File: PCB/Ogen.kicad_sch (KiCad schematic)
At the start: 17 parts, among them J1 Input, U1 PMW3360DM-T2QU, U2 TLV70019, U3 TXS0102DCU, U4 TXS0102DCU, U5 TXS0102DCU

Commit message: V1.2 update.
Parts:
- removed C1: 4.7uF, Capacitor_SMD:C_0603_1608Metric, symbol Device:C_Small
- removed C2: 100nF, Capacitor_SMD:C_0603_1608Metric, symbol Device:C_Small
- removed C3, C4: 1uF, Capacitor_SMD:C_0603_1608Metric, symbol Device:C_Small
- removed R1, R2: 10k, Resistor_SMD:R_0603_1608Metric, symbol Device:R_Small
- removed R3: 39R, Resistor_SMD:R_0603_1608Metric, symbol Device:R_Small
- removed U2: TLV70019, Package_TO_SOT_SMD:SOT-23-5, symbol Regulator_Linear:TLV70019_SOT23-5
- added C22 (x2): 1u, Capacitor_SMD:C_0402_1005Metric, symbol Device:C_Small
- added C93: 4u7, Capacitor_SMD:C_0603_1608Metric, symbol Device:C_Small
- added C94: 100n, Capacitor_SMD:C_0402_1005Metric, symbol Device:C_Small
- added R10, R14, R27: 10k, Resistor_SMD:R_0402_1005Metric, symbol Device:R_Small
- added R11: 39, Resistor_SMD:R_0402_1005Metric, symbol Device:R_Small
- added R28: 15k, Resistor_SMD:R_0402_1005Metric, symbol Device:R_Small
- added U6: AP2127K-ADJ, Package_TO_SOT_SMD:SOT-23-5, symbol Regulator_Linear:AP2127K-ADJ
- A1: footprint Ogen:Ariamelon_Logo -> Ogen:Ariamelon_Logo-CU; symbol Mechanical:MountingHole -> Mechanical:Fiducial
- U3, U4, U5: LCSC (none) -> C53434
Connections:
- net GND: now also C22.2, C22.2, C93.2, C94.1, R27.2, U6.2 (GND)
- net NRESET: now also R10.1
- net VCC: now also C22.1, U6.1 (VIN), U6.3 (EN)
- net at U1.3 (VDDPIX): now also C93.1, C94.2
- net at U1.15 (LED_P): now also R11.1
- net at JP1.1 (A): now also R14.2
- net VDD renamed +2V
- net +2V: now also C22.1, R10.2, R11.2, R14.1, R28.1, U6.5 (VOUT)
- new net: R27.1, R28.2, U6.4 (ADJ)
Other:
- moved on the sheet: H1, H2, J1, JP1, U1, U3, U4, U5

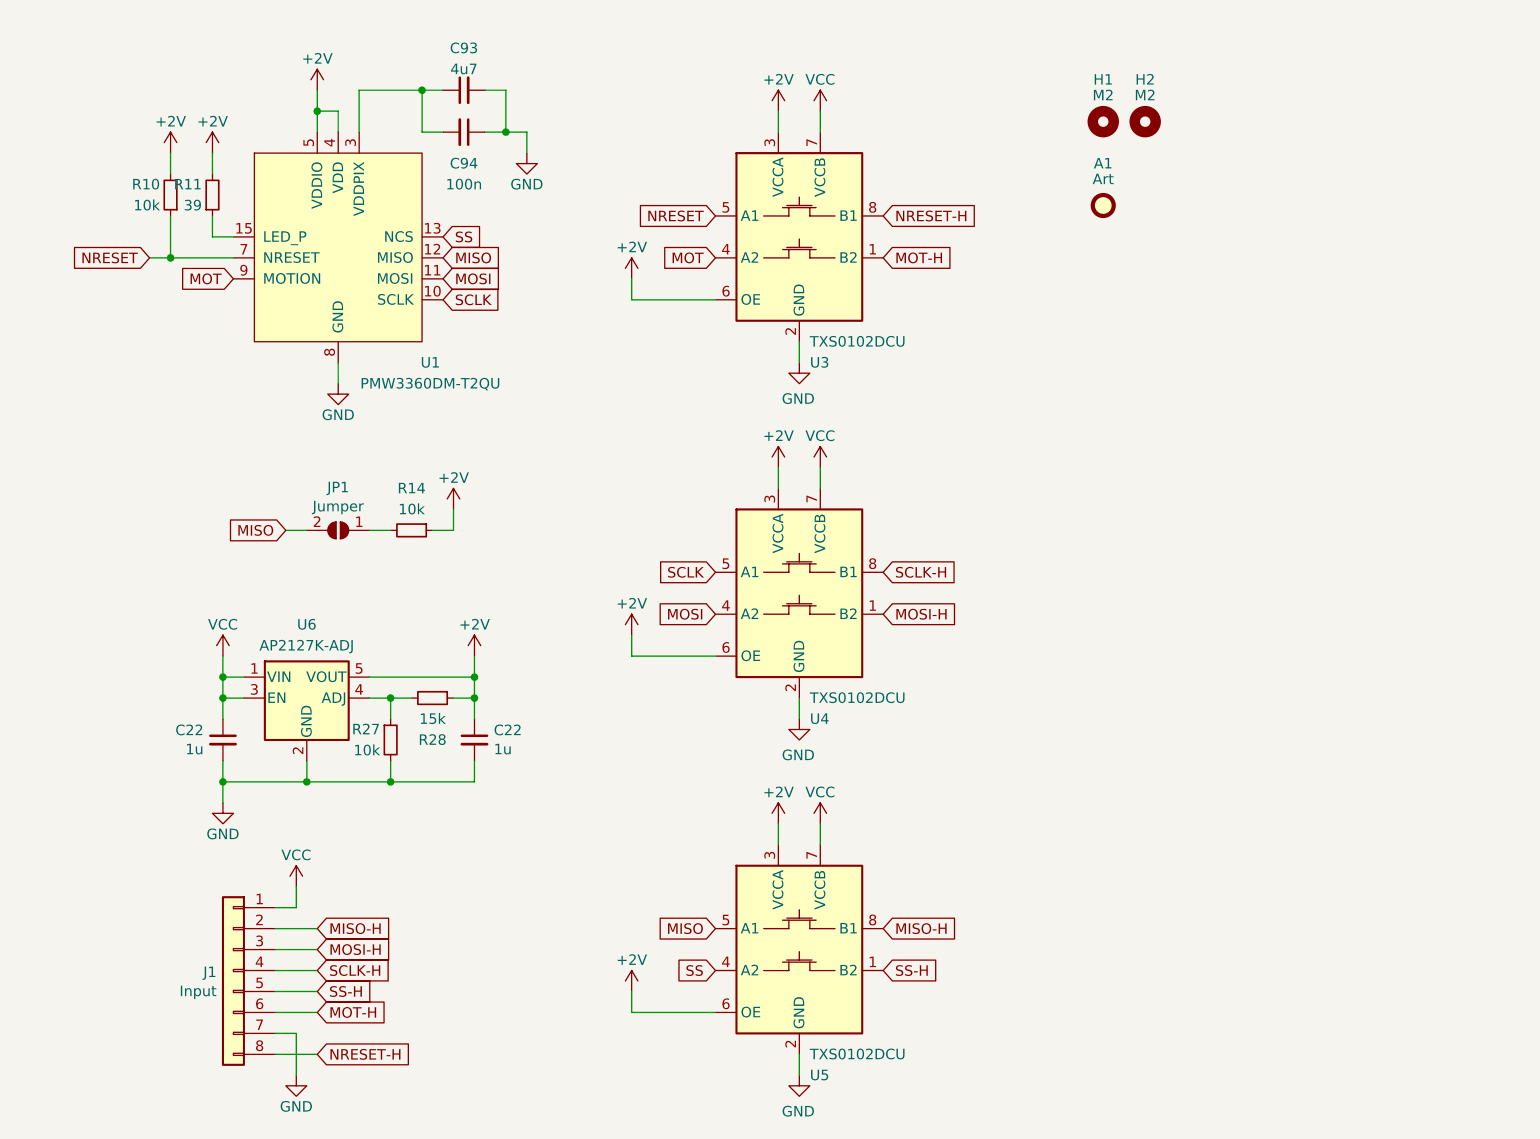
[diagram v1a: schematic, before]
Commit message: 04/08/2023 update
Updated to V1.3. Changed all parts back to 0603. Stitched ground planes together. Removed MISO pullup jumper (MISO is pulled up by default now). Added metadata to schematic and PCB file. Changed location of production files for easier access.
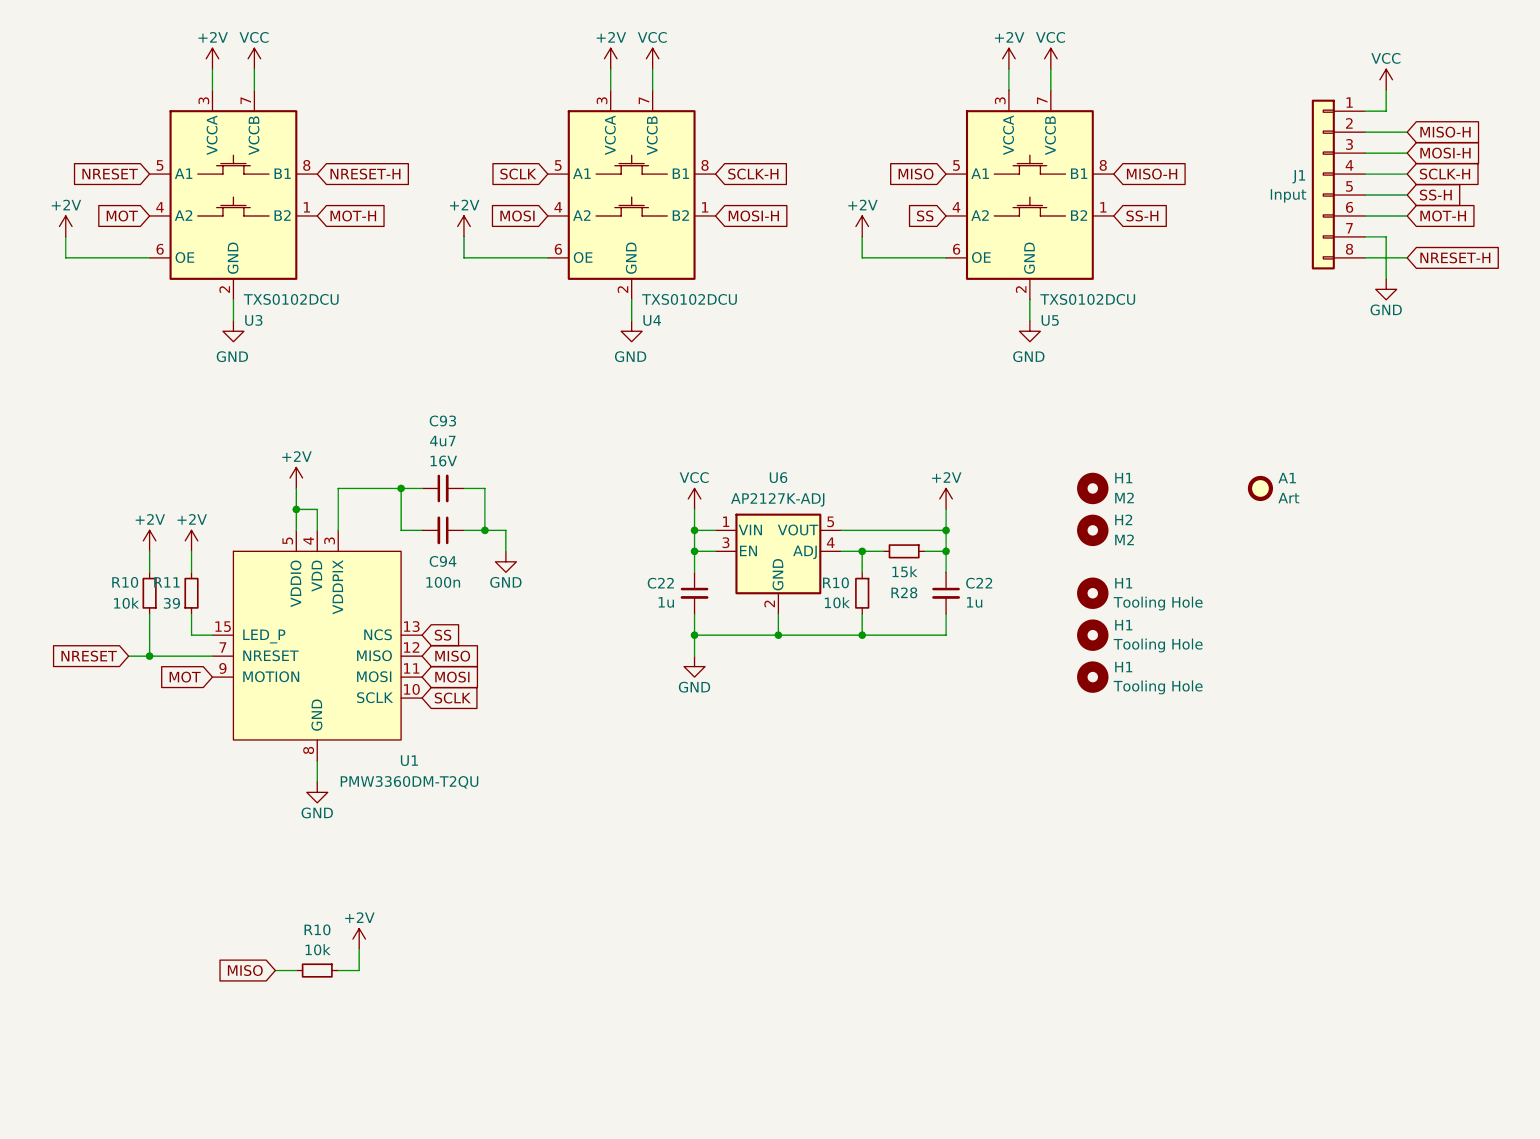
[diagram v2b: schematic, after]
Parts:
- removed JP1: Jumper, Jumper:SolderJumper-2_P1.3mm_Open_Pad1.0x1.5mm, symbol Jumper:SolderJumper_2_Open
- removed R14, R27: 10k, Resistor_SMD:R_0402_1005Metric, symbol Device:R_Small
- added H1 (x3): Tooling Hole, Ogen:JLC Tooling Hole, symbol Mechanical:MountingHole
- added R10 (x2): 10k, Resistor_SMD:R_0603_1608Metric, symbol Device:R_Small
- A1, H1, H2, J1: now left out of the parts list
- C22: footprint Capacitor_SMD:C_0402_1005Metric -> Capacitor_SMD:C_0603_1608Metric; LCSC C52923 -> C15849
- C93: Voltage (none) -> 16V
- C94: footprint Capacitor_SMD:C_0402_1005Metric -> Capacitor_SMD:C_0603_1608Metric; LCSC C1525 -> C14663
- R10: footprint Resistor_SMD:R_0402_1005Metric -> Resistor_SMD:R_0603_1608Metric; LCSC C25744 -> C25804
- R11: footprint Resistor_SMD:R_0402_1005Metric -> Resistor_SMD:R_0603_1608Metric; LCSC C25164 -> C25236
- R28: footprint Resistor_SMD:R_0402_1005Metric -> Resistor_SMD:R_0603_1608Metric; LCSC C25756 -> C22809
- U3, U4, U5: footprint Package_SO:VSSOP-8_2.3x2mm_P0.5mm -> Ogen:VSSOP-8_2.3x2mm_P0.5mm
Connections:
- net +2V: now also R10.1
- net GND: now also R10.2
- net MISO: now also R10.2
- net at R28.2, U6.4 (ADJ): now also R10.1
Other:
- company: (none) -> Created by Ariamelon (https://github.com/Ariamelon/Ogen/tree/V1.3)
- title: (none) -> Ogen PMW3360 Module
- moved on the sheet: A1, C22, C93, C94, H1, H2, J1, R10, R11, R28, U1, U3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

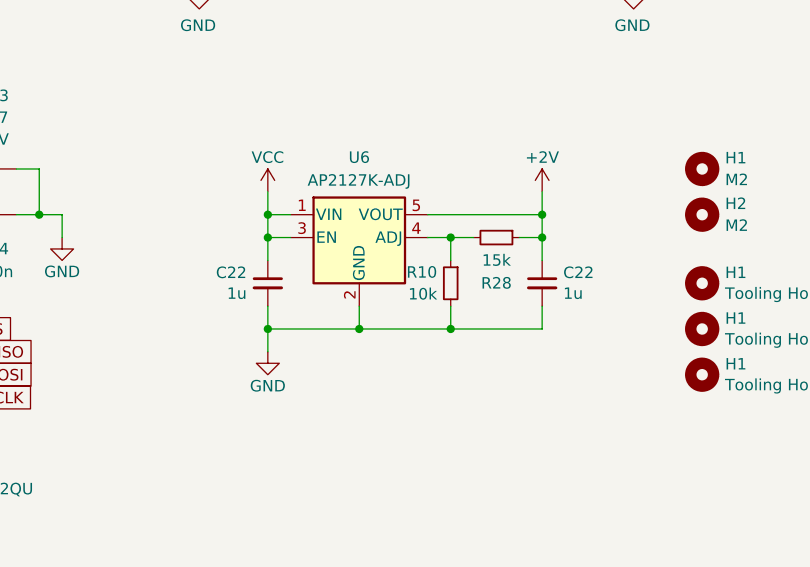
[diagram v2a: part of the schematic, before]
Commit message: 18/09/2023 update
Updated to V1.4. Fixed .gitignore file. Changed LDO capacitors to 4u7 to match the one used in the PMW3360.
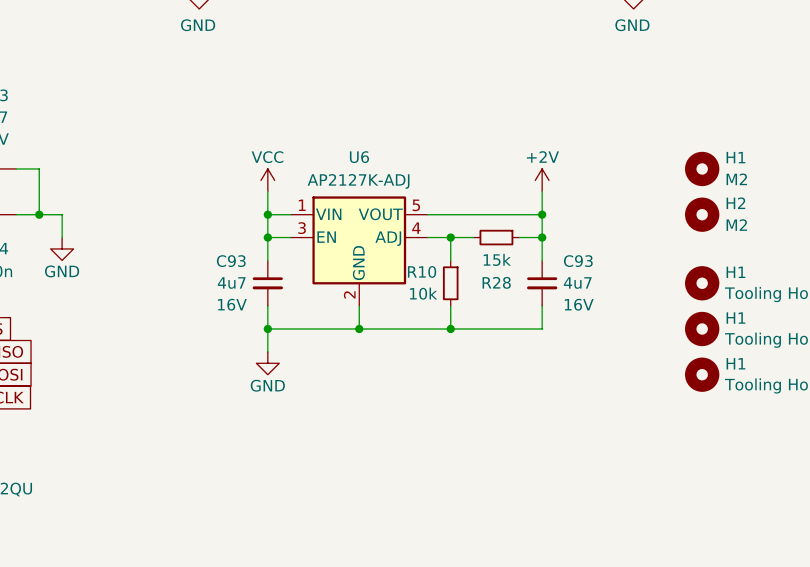
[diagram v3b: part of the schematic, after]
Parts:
- removed C22 (x2): 1u, Capacitor_SMD:C_0603_1608Metric, symbol Device:C_Small
- added C93 (x2): 4u7, Capacitor_SMD:C_0603_1608Metric, symbol Device:C_Small
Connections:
- net +2V: now also C93.1
- net GND: now also C93.2, C93.2
- net VCC: now also C93.1
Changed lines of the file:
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@@
   (title_block
     (title "Ogen PMW3360 Module")
-    (date "2023-08-04")
-    (rev "V1.3")
+    (date "2023-09-18")
+    (rev "V1.4")
     (company "Created by Ariamelon (https://github.com/Ariamelon/Ogen/tree/V1.3)")
     (comment 1 "All capacitors 50V unless otherwise specified.")
@@
         (path "/ee41cb8e-512d-41d2-81e1-3c50fff32aeb"
           (reference "H1") (unit 1)
+        )
+      )
+    )
+  )
+  (symbol (lib_id "Device:C_Small") (at 93.98 83.82 0) (unit 1)
+    (in_bom yes) (on_board yes) (dnp no) (fields_autoplaced)
+    (property "Reference" "C93" (at 91.6559 81.4021 0)
+      (effects (font (size 1.27 1.27)) (justify right))
+    )
+    (property "Value" "4u7" (at 91.6559 83.8263 0)
+      (effects (font (size 1.27 1.27)) (justify right))
+    )
+    (property "Footprint" "Capacitor_SMD:C_0603_1608Metric" (at 93.98 83.82 0)
+      (effects (font (size 1.27 1.27)) hide)
+    )
+    (property "Datasheet" "~" (at 93.98 83.82 0)
+      (effects (font (size 1.27 1.27)) hide)
+    )
+    (property "Description" "0603 capacitor" (at 93.98 83.82 0)
+      (effects (font (size 1.27 1.27)) hide)
+    )
+    (property "LCSC" "C19666" (at 93.98 83.82 0)
+      (effects (font (size 1.27 1.27)) hide)
+    )
+    (property "Voltage" "16V" (at 91.6559 86.2505 0)
+      (effects (font (size 1.27 1.27)) (justify right))
+    )
+    (pin "1")
+    (pin "2")
+    (instances
+      (project "Honeydew"
+        (path "/534caec7-cf60-4f90-b1ed-42c9d445ef0f/3b9d6b66-6ecb-42d2-a8a6-a52a8ef176c3"
+          (reference "C93") (unit 1)
+        )
+      )
+      (project "Ogen"
+        (path "/ee41cb8e-512d-41d2-81e1-3c50fff32aeb"
+          (reference "C3") (unit 1)
         )
       )
@@
     )
   )
+  (symbol (lib_id "Device:C_Small") (at 124.46 83.82 0) (unit 1)
+    (in_bom yes) (on_board yes) (dnp no) (fields_autoplaced)
+    (property "Reference" "C93" (at 126.7841 81.4021 0)
+      (effects (font (size 1.27 1.27)) (justify left))
+    )
+    (property "Value" "4u7" (at 126.7841 83.8263 0)
+      (effects (font (size 1.27 1.27)) (justify left))
+    )
+    (property "Footprint" "Capacitor_SMD:C_0603_1608Metric" (at 124.46 83.82 0)
+      (effects (font (size 1.27 1.27)) hide)
+    )
+    (property "Datasheet" "~" (at 124.46 83.82 0)
+      (effects (font (size 1.27 1.27)) hide)
+    )
+    (property "Description" "0603 capacitor" (at 124.46 83.82 0)
+      (effects (font (size 1.27 1.27)) hide)
+    )
+    (property "LCSC" "C19666" (at 124.46 83.82 0)
+      (effects (font (size 1.27 1.27)) hide)
+    )
+    (property "Voltage" "16V" (at 126.7841 86.2505 0)
+      (effects (font (size 1.27 1.27)) (justify left))
+    )
+    (pin "1")
+    (pin "2")
+    (instances
+      (project "Honeydew"
+        (path "/534caec7-cf60-4f90-b1ed-42c9d445ef0f/3b9d6b66-6ecb-42d2-a8a6-a52a8ef176c3"
+          (reference "C93") (unit 1)
+        )
+      )
+      (project "Ogen"
+        (path "/ee41cb8e-512d-41d2-81e1-3c50fff32aeb"
+          (reference "C4") (unit 1)
+        )
+      )
+    )
+  )
   (symbol (lib_id "power:GND") (at 86.36 50.8 0) (mirror y) (unit 1)
     (in_bom yes) (on_board yes) (dnp no)
@@
     )
   )
-  (symbol (lib_id "Device:C_Small") (at 124.46 83.82 0) (unit 1)
-    (in_bom yes) (on_board yes) (dnp no) (fields_autoplaced)
-    (property "Reference" "C22" (at 126.7968 82.6516 0)
-      (effects (font (size 1.27 1.27)) (justify left))
-    )
-    (property "Value" "1u" (at 126.7968 84.963 0)
-      (effects (font (size 1.27 1.27)) (justify left))
-    )
-    (property "Footprint" "Capacitor_SMD:C_0603_1608Metric" (at 124.46 83.82 0)
-      (effects (font (size 1.27 1.27)) hide)
-    )
-    (property "Datasheet" "~" (at 124.46 83.82 0)
-      (effects (font (size 1.27 1.27)) hide)
-    )
-    (property "Description" "0603 capacitor" (at 124.46 83.82 0)
-      (effects (font (size 1.27 1.27)) hide)
-    )
-    (property "LCSC" "C15849" (at 124.46 83.82 0)
-      (effects (font (size 1.27 1.27)) hide)
-    )
-    (pin "1")
-    (pin "2")
-    (instances
-      (project "Honeydew"
-        (path "/534caec7-cf60-4f90-b1ed-42c9d445ef0f/0e23afb1-1d24-49d7-b6b4-dea31b732359"
-          (reference "C22") (unit 1)
-        )
-      )
-      (project "Ogen"
-        (path "/ee41cb8e-512d-41d2-81e1-3c50fff32aeb"
-          (reference "C4") (unit 1)
-        )
-      )
-    )
-  )
   (symbol (lib_id "Mechanical:MountingHole") (at 142.24 93.98 0) (unit 1)
     (in_bom no) (on_board yes) (dnp no)
@@
         )
       )
-    )
-  )
-  (symbol (lib_id "Device:C_Small") (at 93.98 83.82 0) (mirror y) (unit 1)
-    (in_bom yes) (on_board yes) (dnp no)
-    (property "Reference" "C22" (at 91.6432 82.6516 0)
-      (effects (font (size 1.27 1.27)) (justify left))
-    )
-    (property "Value" "1u" (at 91.6432 84.963 0)
-      (effects (font (size 1.27 1.27)) (justify left))
-    )
-    (property "Footprint" "Capacitor_SMD:C_0603_1608Metric" (at 93.98 83.82 0)
-      (effects (font (size 1.27 1.27)) hide)
-    )
-    (property "Datasheet" "~" (at 93.98 83.82 0)
-      (effects (font (size 1.27 1.27)) hide)
-    )
-    (property "Description" "0603 capacitor" (at 93.98 83.82 0)
-      (effects (font (size 1.27 1.27)) hide)
-    )
-    (property "LCSC" "C15849" (at 93.98 83.82 0)
-      (effects (font (size 1.27 1.27)) hide)
-    )
-    (pin "1")
-    (pin "2")
-    (instances
-      (project "Honeydew"
-        (path "/534caec7-cf60-4f90-b1ed-42c9d445ef0f/0e23afb1-1d24-49d7-b6b4-dea31b732359"
-          (reference "C22") (unit 1)
-        )
-      )
-      (project "Ogen"
-        (path "/ee41cb8e-512d-41d2-81e1-3c50fff32aeb"
-          (reference "C3") (unit 1)
-        )
-      )

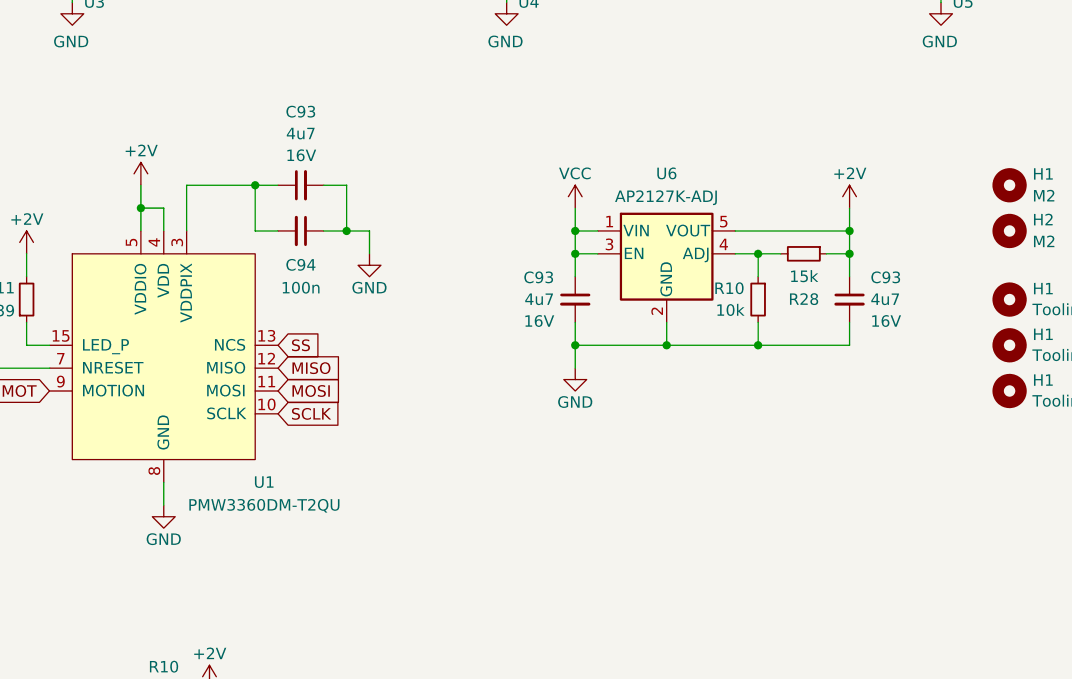
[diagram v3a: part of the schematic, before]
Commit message: V1.5 update
Changed LDO to XC6206P202MR. Unified libraries with master library.
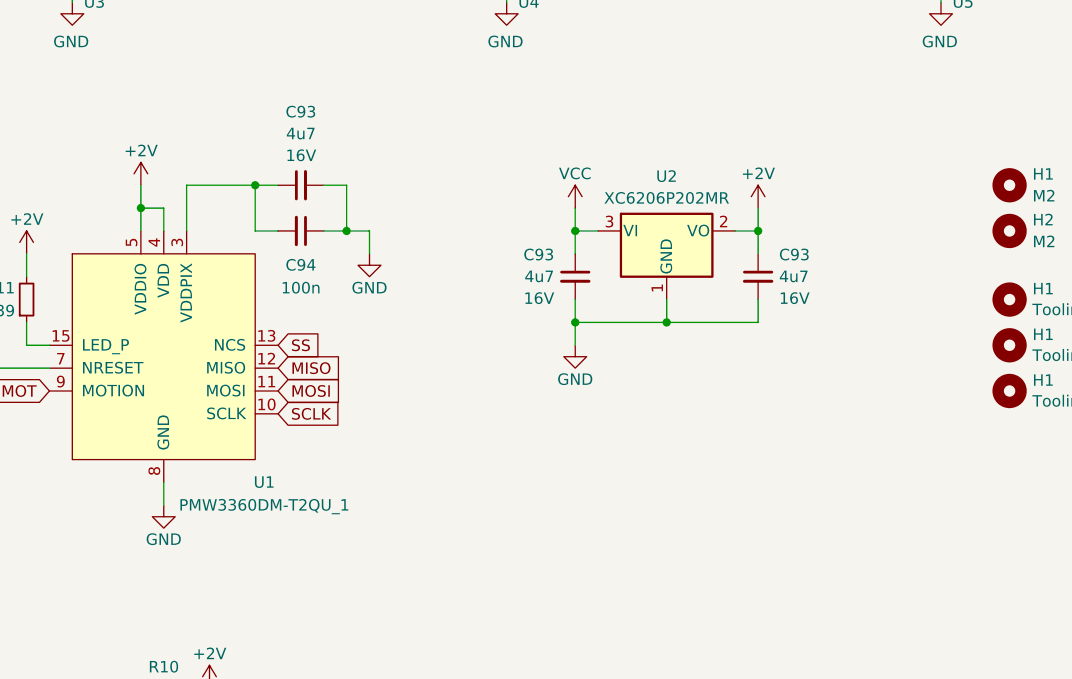
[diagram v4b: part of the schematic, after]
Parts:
- removed R10: 10k, Resistor_SMD:R_0603_1608Metric, symbol Device:R_Small
- removed R28: 15k, Resistor_SMD:R_0603_1608Metric, symbol Device:R_Small
- removed U6: AP2127K-ADJ, Package_TO_SOT_SMD:SOT-23-5, symbol Regulator_Linear:AP2127K-ADJ
- added U2: XC6206P202MR, Ariamelon-Package:SOT-23-3, symbol Regulator_Linear:XC6206PxxxMR
- U1: value PMW3360DM-T2QU -> PMW3360DM-T2QU_1; symbol Ogen:PMW3360DM-T2QU -> Ariamelon-IC:PMW3360DM-T2QU_1
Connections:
- net +2V: now also U2.2 (VO)
- net GND: now also U2.1 (GND)
- net VCC: now also U2.3 (VI)
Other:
- moved on the sheet: C93
